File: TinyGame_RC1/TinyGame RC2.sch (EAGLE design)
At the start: 45 parts, among them J1 AUDIO-CONNECTOR-6P-SMD-344003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, K1 BUTTON-4P-3100010P1, K2 BUTTON-4P-3100010P1, K3 BUTTON-4P-3100010P1, K4 BUTTON-4P-3100010P1, U1 MKL02Z32VFK4

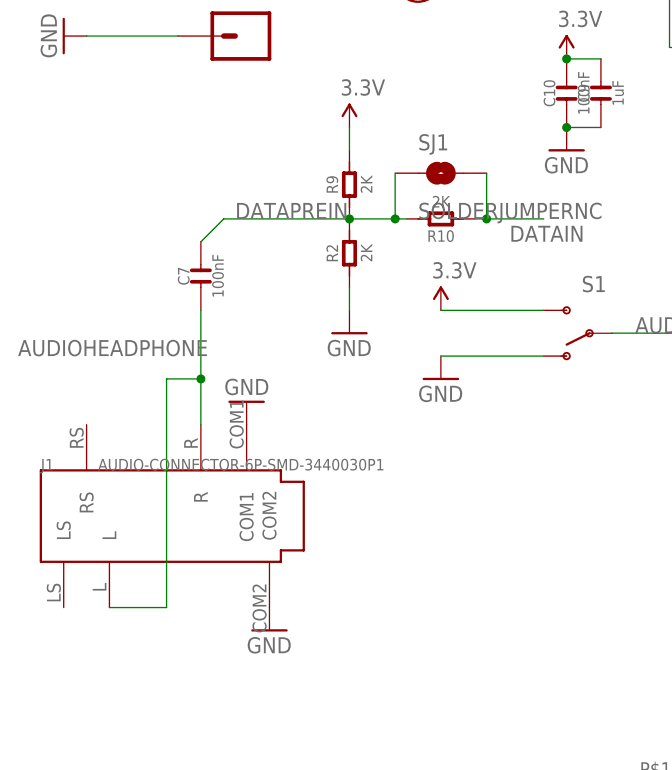
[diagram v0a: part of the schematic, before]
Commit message: RC2 design update for programming
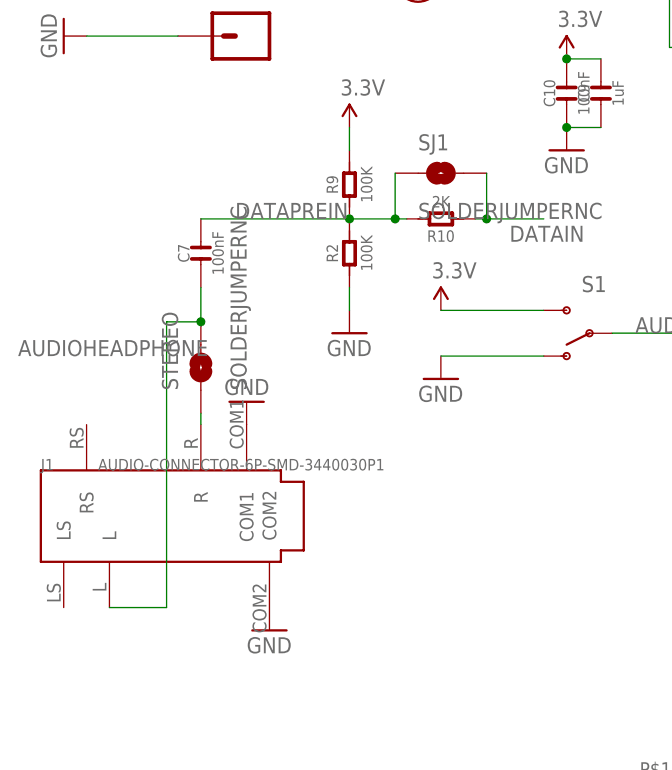
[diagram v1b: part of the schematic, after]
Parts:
- added STEREO: SOLDERJUMPERNC, SparkFun-Passives:SOLDERJUMPERNC
- R2, R9: value 2K -> 100K
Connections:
- net N$20 renamed VBAT
- new net N$1: J1.R, STEREO.1
- net AUDIOHEADPHONE: now also STEREO.2; no longer J1.R
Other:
- moved on the sheet: C7
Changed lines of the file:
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@@
 <?xml version="1.0" encoding="utf-8"?>
 <!DOCTYPE eagle SYSTEM "eagle.dtd">
-<eagle version="6.5.0">
+<eagle version="7.7.0">
 <drawing>
 <settings>
@@
 <part name="SUPPLY9" library="SparkFun-Aesthetics" deviceset="3.3V" device=""/>
 <part name="GND16" library="SparkFun-Aesthetics" deviceset="GND" device=""/>
-<part name="R2" library="OPL" deviceset="R*" device="-0603" value="2K"/>
-<part name="R9" library="OPL" deviceset="R*" device="-0603" value="2K"/>
+<part name="R2" library="OPL" deviceset="R*" device="-0603" value="100K"/>
+<part name="R9" library="OPL" deviceset="R*" device="-0603" value="100K"/>
 <part name="R10" library="OPL" deviceset="R*" device="-0603" value="2K"/>
 <part name="C7" library="OPL" deviceset="C*" device="-0603" value="100nF"/>
 <part name="SJ1" library="SparkFun-Passives" deviceset="SOLDERJUMPER" device="NC"/>
+<part name="STEREO" library="SparkFun-Passives" deviceset="SOLDERJUMPER" device="NC"/>
 </parts>
 <sheets>
@@
 <instance part="R9" gate="R" x="85.09" y="49.53" rot="R90"/>
 <instance part="R10" gate="R" x="95.25" y="45.72" rot="R180"/>
-<instance part="C7" gate="C" x="68.58" y="39.37" rot="R90"/>
+<instance part="C7" gate="C" x="68.58" y="41.91" rot="R90"/>
 <instance part="SJ1" gate="1" x="95.25" y="50.8"/>
+<instance part="STEREO" gate="1" x="68.58" y="29.21" rot="R90"/>
 </instances>
 <busses>
@@
 </segment>
 </net>
-<net name="N$20" class="0">
+<net name="VBAT" class="0">
 <segment>
 <wire x1="120.65" y1="71.12" x2="120.65" y2="64.77" width="0.1524" layer="91"/>
@@
 </segment>
 <segment>
-<pinref part="J1" gate="J" pin="R"/>
-<wire x1="68.58" y1="35.56" x2="68.58" y2="27.94" width="0.1524" layer="91"/>
+<wire x1="68.58" y1="38.1" x2="68.58" y2="34.29" width="0.1524" layer="91"/>
 <pinref part="J1" gate="J" pin="L"/>
-<wire x1="68.58" y1="27.94" x2="68.58" y2="22.86" width="0.1524" layer="91"/>
 <wire x1="58.42" y1="2.54" x2="64.77" y2="2.54" width="0.1524" layer="91"/>
-<wire x1="64.77" y1="2.54" x2="64.77" y2="27.94" width="0.1524" layer="91"/>
-<wire x1="64.77" y1="27.94" x2="68.58" y2="27.94" width="0.1524" layer="91"/>
-<junction x="68.58" y="27.94"/>
+<wire x1="64.77" y1="2.54" x2="64.77" y2="34.29" width="0.1524" layer="91"/>
+<wire x1="64.77" y1="34.29" x2="68.58" y2="34.29" width="0.1524" layer="91"/>
 <label x="48.26" y="30.48" size="1.778" layer="95"/>
 <pinref part="C7" gate="C" pin="1"/>
+<pinref part="STEREO" gate="1" pin="2"/>
+<junction x="68.58" y="34.29"/>
 </segment>
 </net>
 <net name="DATAPREIN" class="0">
 <segment>
-<wire x1="68.58" y1="43.18" x2="71.12" y2="45.72" width="0.1524" layer="91"/>
-<wire x1="71.12" y1="45.72" x2="85.09" y2="45.72" width="0.1524" layer="91"/>
+<wire x1="68.58" y1="45.72" x2="85.09" y2="45.72" width="0.1524" layer="91"/>
 <label x="72.39" y="45.72" size="1.778" layer="95"/>
 <pinref part="R2" gate="R" pin="2"/>
@@
 </segment>
 </net>
+<net name="N$1" class="0">
+<segment>
+<pinref part="J1" gate="J" pin="R"/>
+<pinref part="STEREO" gate="1" pin="1"/>
+<wire x1="68.58" y1="24.13" x2="68.58" y2="22.86" width="0.1524" layer="91"/>
+</segment>
+</net>
